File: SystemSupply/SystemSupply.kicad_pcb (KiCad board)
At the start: 2 copper layers, 75 x 75 mm, 44 parts, among them J1 Conn_01x01, J10 Screw_Terminal_01x02, J2 Conn_01x01, J3 4P4C, J4 Conn_01x01, J5 Conn_01x01, J6 Screw_Terminal_01x02, J7 4P4C, J8 Screw_Terminal_01x02, J9 Screw_Terminal_01x02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

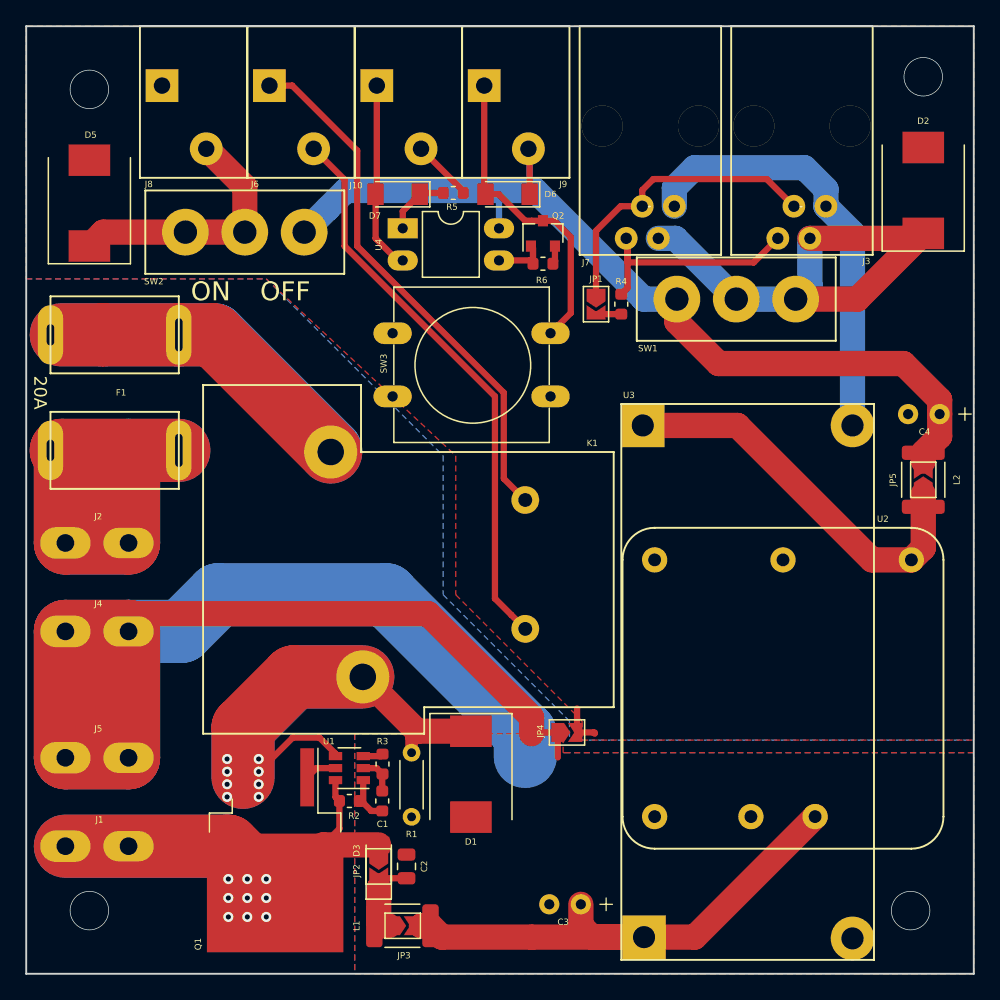
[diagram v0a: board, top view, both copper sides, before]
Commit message: Added grounding vias in SystemSupply.
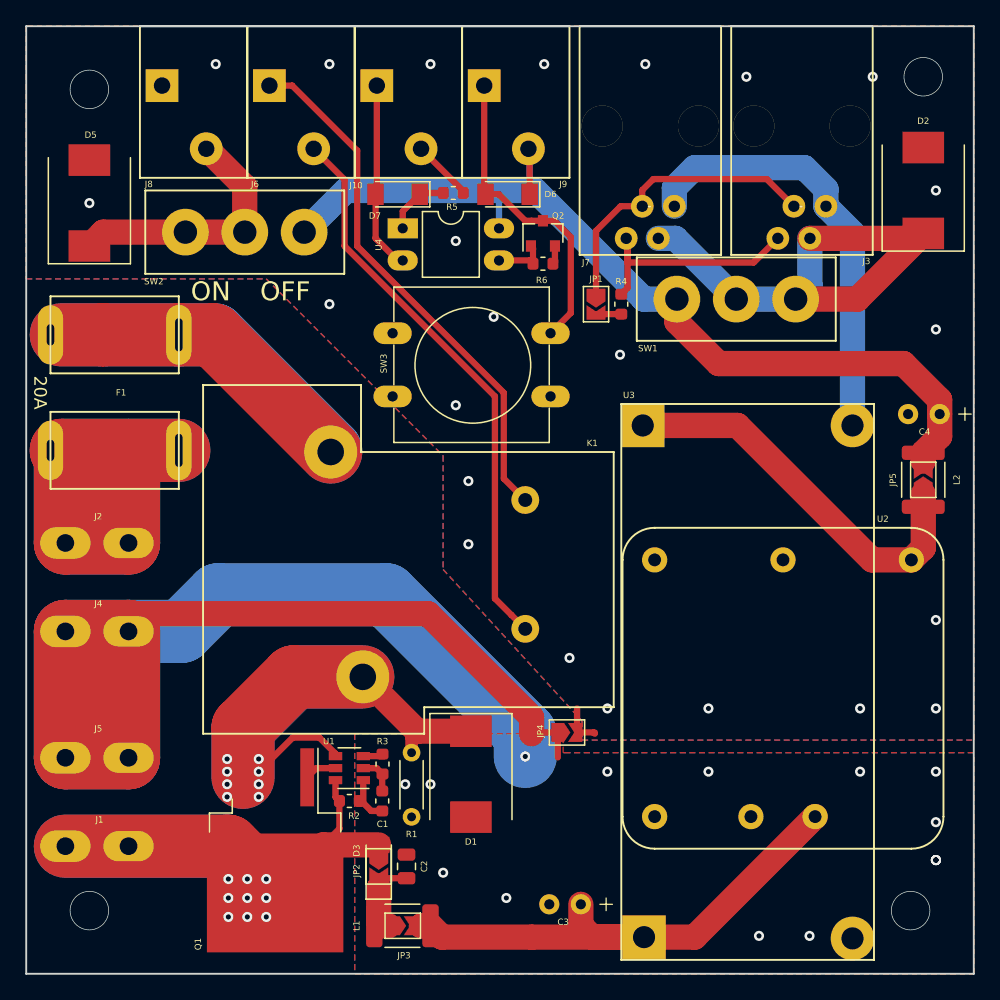
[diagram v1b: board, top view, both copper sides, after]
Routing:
- net GNDPWR: vias 0 -> 15
- net GND: vias 0 -> 23
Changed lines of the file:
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@@
     (thickness 1.6)
     (drawings 7)
-    (tracks 225)
+    (tracks 264)
     (zones 0)
     (modules 44)
@@
   )
   (setup
-    (last_trace_width 0.5)
+    (last_trace_width 0.25)
     (user_trace_width 0.3)
     (user_trace_width 0.5)
@@
   (via (at 131 94) (size 3.1) (drill 3) (layers F.Cu B.Cu) (net 0))
   (via (at 65 95) (size 3.1) (drill 3) (layers F.Cu B.Cu) (net 0))
-  (via (at 76 157.5) (size 0.8) (drill 0.4) (layers F.Cu B.Cu) (net 6))
-  (via (at 76 159) (size 0.8) (drill 0.4) (layers F.Cu B.Cu) (net 6))
-  (via (at 77.5 157.5) (size 0.8) (drill 0.4) (layers F.Cu B.Cu) (net 6))
-  (via (at 79 157.5) (size 0.8) (drill 0.4) (layers F.Cu B.Cu) (net 6))
-  (via (at 79 159) (size 0.8) (drill 0.4) (layers F.Cu B.Cu) (net 6))
-  (via (at 77.5 159) (size 0.8) (drill 0.4) (layers F.Cu B.Cu) (net 6))
-  (via (at 79 160.5) (size 0.8) (drill 0.4) (layers F.Cu B.Cu) (net 6))
-  (via (at 76 160.5) (size 0.8) (drill 0.4) (layers F.Cu B.Cu) (net 6))
   (via (at 75.9 148) (size 0.8) (drill 0.4) (layers F.Cu B.Cu) (net 1))
   (via (at 75.9 151) (size 0.8) (drill 0.4) (layers F.Cu B.Cu) (net 1))
@@
   (segment (start 75.185045 135) (end 88.5 135) (width 5) (layer B.Cu) (net 2))
   (segment (start 72.285045 137.9) (end 75.185045 135) (width 5) (layer B.Cu) (net 2))
+  (via (at 122 162) (size 0.8) (drill 0.4) (layers F.Cu B.Cu) (net 2))
+  (via (at 118 162) (size 0.8) (drill 0.4) (layers F.Cu B.Cu) (net 2))
+  (via (at 132 156) (size 0.8) (drill 0.4) (layers F.Cu B.Cu) (net 2))
+  (via (at 132 156) (size 0.8) (drill 0.4) (layers F.Cu B.Cu) (net 2))
+  (via (at 132 156) (size 0.8) (drill 0.4) (layers F.Cu B.Cu) (net 2))
+  (via (at 132 153) (size 0.8) (drill 0.4) (layers F.Cu B.Cu) (net 2))
+  (via (at 132 149) (size 0.8) (drill 0.4) (layers F.Cu B.Cu) (net 2))
+  (via (at 126 149) (size 0.8) (drill 0.4) (layers F.Cu B.Cu) (net 2))
+  (via (at 114 149) (size 0.8) (drill 0.4) (layers F.Cu B.Cu) (net 2))
+  (via (at 106 149) (size 0.8) (drill 0.4) (layers F.Cu B.Cu) (net 2))
+  (segment (start 99.5 147.8) (end 99.5 147.8) (width 5) (layer B.Cu) (net 2))
+  (via (at 99.5 147.8) (size 0.8) (drill 0.4) (layers F.Cu B.Cu) (net 2))
+  (via (at 98 159) (size 0.8) (drill 0.4) (layers F.Cu B.Cu) (net 2))
+  (via (at 93 157) (size 0.8) (drill 0.4) (layers F.Cu B.Cu) (net 2))
+  (via (at 92 150) (size 0.8) (drill 0.4) (layers F.Cu B.Cu) (net 2))
+  (via (at 90 150) (size 0.8) (drill 0.4) (layers F.Cu B.Cu) (net 2))
   (segment (start 99.8525 108.54) (end 100.1125 108.8) (width 0.5) (layer F.Cu) (net 3))
   (segment (start 97.42 108.54) (end 99.8525 108.54) (width 0.5) (layer F.Cu) (net 3))
@@
   (segment (start 103.625 145.9) (end 105 145.9) (width 0.5) (layer F.Cu) (net 4))
   (segment (start 103.6 145.925) (end 103.6 144) (width 0.5) (layer F.Cu) (net 4))
+  (via (at 132 144) (size 0.8) (drill 0.4) (layers F.Cu B.Cu) (net 4))
+  (via (at 126 144) (size 0.8) (drill 0.4) (layers F.Cu B.Cu) (net 4))
+  (via (at 114 144) (size 0.8) (drill 0.4) (layers F.Cu B.Cu) (net 4))
+  (via (at 106 144) (size 0.8) (drill 0.4) (layers F.Cu B.Cu) (net 4))
+  (via (at 103 140) (size 0.8) (drill 0.4) (layers F.Cu B.Cu) (net 4))
+  (via (at 132 137) (size 0.8) (drill 0.4) (layers F.Cu B.Cu) (net 4))
+  (via (at 132 114) (size 0.8) (drill 0.4) (layers F.Cu B.Cu) (net 4))
+  (via (at 132 103) (size 0.8) (drill 0.4) (layers F.Cu B.Cu) (net 4))
+  (via (at 127 94) (size 0.8) (drill 0.4) (layers F.Cu B.Cu) (net 4))
+  (via (at 117 94) (size 0.8) (drill 0.4) (layers F.Cu B.Cu) (net 4))
+  (via (at 109 93) (size 0.8) (drill 0.4) (layers F.Cu B.Cu) (net 4))
+  (via (at 101 93) (size 0.8) (drill 0.4) (layers F.Cu B.Cu) (net 4))
+  (via (at 92 93) (size 0.8) (drill 0.4) (layers F.Cu B.Cu) (net 4))
+  (via (at 84 93) (size 0.8) (drill 0.4) (layers F.Cu B.Cu) (net 4))
+  (via (at 75 93) (size 0.8) (drill 0.4) (layers F.Cu B.Cu) (net 4))
+  (via (at 65 104) (size 0.8) (drill 0.4) (layers F.Cu B.Cu) (net 4))
+  (via (at 95 131) (size 0.8) (drill 0.4) (layers F.Cu B.Cu) (net 4))
+  (via (at 95 126) (size 0.8) (drill 0.4) (layers F.Cu B.Cu) (net 4))
+  (via (at 94 120) (size 0.8) (drill 0.4) (layers F.Cu B.Cu) (net 4))
+  (via (at 84 112) (size 0.8) (drill 0.4) (layers F.Cu B.Cu) (net 4))
+  (via (at 94 107) (size 0.8) (drill 0.4) (layers F.Cu B.Cu) (net 4))
+  (via (at 97 113) (size 0.8) (drill 0.4) (layers F.Cu B.Cu) (net 4))
+  (via (at 107 116) (size 0.8) (drill 0.4) (layers F.Cu B.Cu) (net 4))
   (segment (start 86.679482 151.010376) (end 86.366982 151.322876) (width 0.25) (layer F.Cu) (net 5))
   (segment (start 87.310376 152.110376) (end 88.179482 152.110376) (width 0.5) (layer F.Cu) (net 5))
   (segment (start 86.679482 149.672876) (end 86.679482 151.479482) (width 0.5) (layer F.Cu) (net 5))
   (segment (start 86.679482 151.479482) (end 87.310376 152.110376) (width 0.5) (layer F.Cu) (net 5))
+  (via (at 76 157.5) (size 0.8) (drill 0.4) (layers F.Cu B.Cu) (net 6))
+  (via (at 76 159) (size 0.8) (drill 0.4) (layers F.Cu B.Cu) (net 6))
+  (via (at 77.5 157.5) (size 0.8) (drill 0.4) (layers F.Cu B.Cu) (net 6))
+  (via (at 79 157.5) (size 0.8) (drill 0.4) (layers F.Cu B.Cu) (net 6))
+  (via (at 79 159) (size 0.8) (drill 0.4) (layers F.Cu B.Cu) (net 6))
+  (via (at 77.5 159) (size 0.8) (drill 0.4) (layers F.Cu B.Cu) (net 6))
+  (via (at 79 160.5) (size 0.8) (drill 0.4) (layers F.Cu B.Cu) (net 6))
+  (via (at 76 160.5) (size 0.8) (drill 0.4) (layers F.Cu B.Cu) (net 6))
   (segment (start 78.6 157.5) (end 77.5 160.5) (width 5) (layer F.Cu) (net 6))
   (segment (start 83.5 154.8) (end 79.7 158.6) (width 2) (layer F.Cu) (net 6))
@@
       (pts
         (xy 135 146.5) (xy 135 90) (xy 60 90) (xy 60 110) (xy 79 110)
-        (xy 94 124) (xy 94 135) (xy 104 145) (xy 104 146.5)
-      )
-    )
-  )
-  (zone (net 4) (net_name GND) (layer B.Cu) (hatch edge 0.508)
-    (connect_pads (clearance 0.508))
-    (min_thickness 0.254)
-    (fill yes (arc_segments 16) (thermal_gap 0.508) (thermal_bridge_width 0.508))
-    (polygon
-      (pts
-        (xy 135 146.5) (xy 135 90) (xy 60 90) (xy 60 110) (xy 79 110)
-        (xy 93 124) (xy 93 135) (xy 103 145) (xy 103 146.5)
+        (xy 93 124) (xy 93 133) (xy 104 145) (xy 104 146.5)
       )
     )
@@
       )
     )
+  )
+  (zone (net 4) (net_name GND) (layer B.Cu) (hatch edge 0.508)
+    (connect_pads (clearance 0.508))
+    (min_thickness 0.254)
+    (fill yes (arc_segments 16) (thermal_gap 0.508) (thermal_bridge_width 0.508))
+    (polygon
+      (pts
+        (xy 135 146.5) (xy 135 90) (xy 60 90) (xy 60 110) (xy 79 110)
+        (xy 93 124) (xy 93 133) (xy 104 145) (xy 104 146.5)
+      )
+    )

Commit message: First review. Fixed polygon pours, silkscreen and soldermask.
Squashed commit of the following:

commit 42a4a5d146683d2b2a8899b51cbc9eaef6797660
Author: Paweł <mackipawel@gmail.com>
Date:   Tue Apr 16 00:20:58 2019 +0200

    Changed solder mask design rules. Changed polygon pours clearence.

commit a27d25858da40b0edc55a62741cad58f571e73a1
Author: Paweł <mackipawel@gmail.com>
Date:   Sun Apr 14 15:00:25 2019 +0200

    Set via size to 0.3/0.6. Added silk screen descriptions in MotorDriver.

commit d55559f2128c74f860d75a89ad8b68139a6ba707
Author: Paweł <mackipawel@gmail.com>
Date:   Sun Apr 14 13:56:25 2019 +0200

    Added EcoTech logo in MotorController.
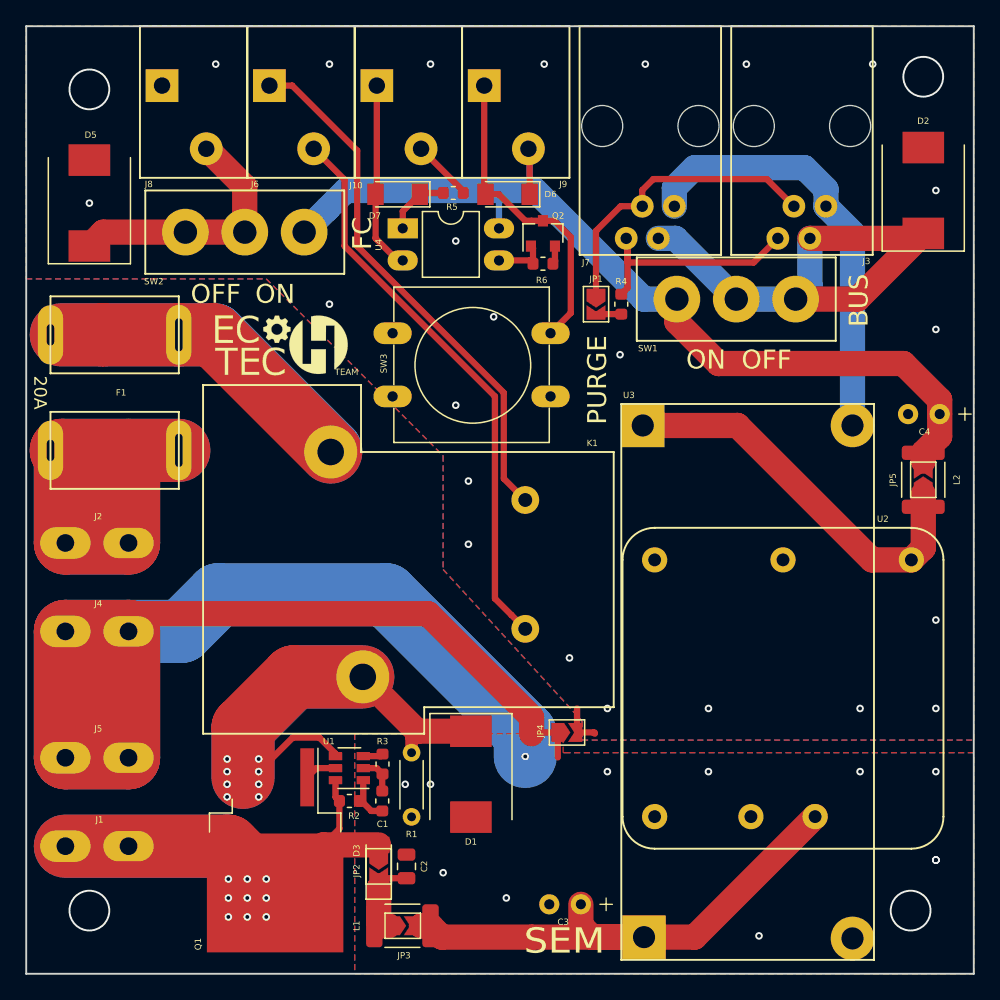
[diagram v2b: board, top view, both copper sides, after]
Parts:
- added G***: LOGO, Footprints:EcoTech, F.Cu at (80.3, 115.5)
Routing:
- net GNDPWR: vias 15 -> 13
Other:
- net class Default: via_dia 0.8 -> 0.6; via_drill 0.4 -> 0.3
- rule pad_to_mask_clearance: 0.051 -> 0.1
- rule solder_mask_min_width: 0.25 -> 0.2
- board text added: "BUS"
- board text added: "FC"
- board text added: "PURGE"
- board text added: "SEM"
